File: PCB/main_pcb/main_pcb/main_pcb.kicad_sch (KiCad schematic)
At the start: 51 parts, among them J1 Conn_01x20_Socket, J2 Conn_01x20_Socket, J3 Conn_01x09_Socket, SW0_Header1 B6B-XH-A, SW1_Header1 B6B-XH-A

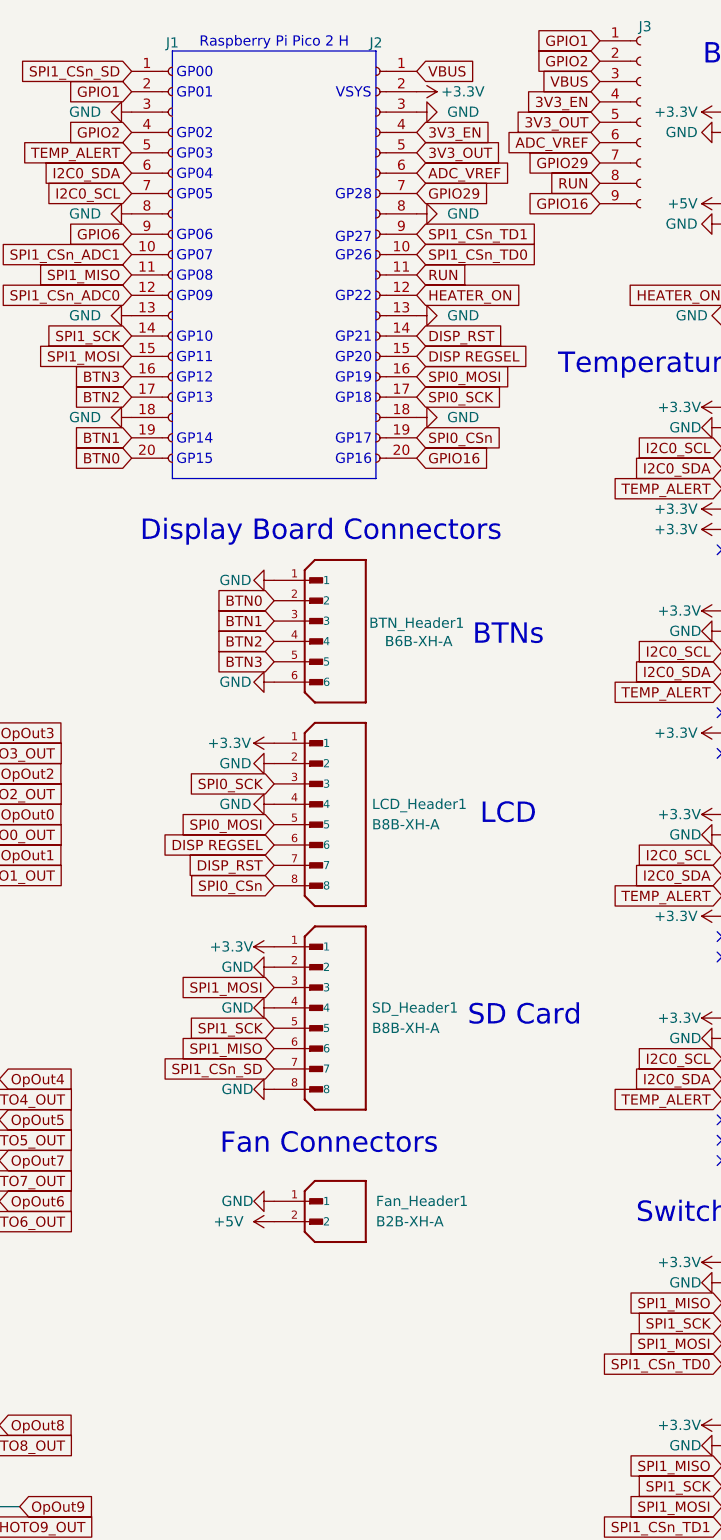
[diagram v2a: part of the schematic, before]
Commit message: Fully seperated analog ground from digital ground on the main PCB.
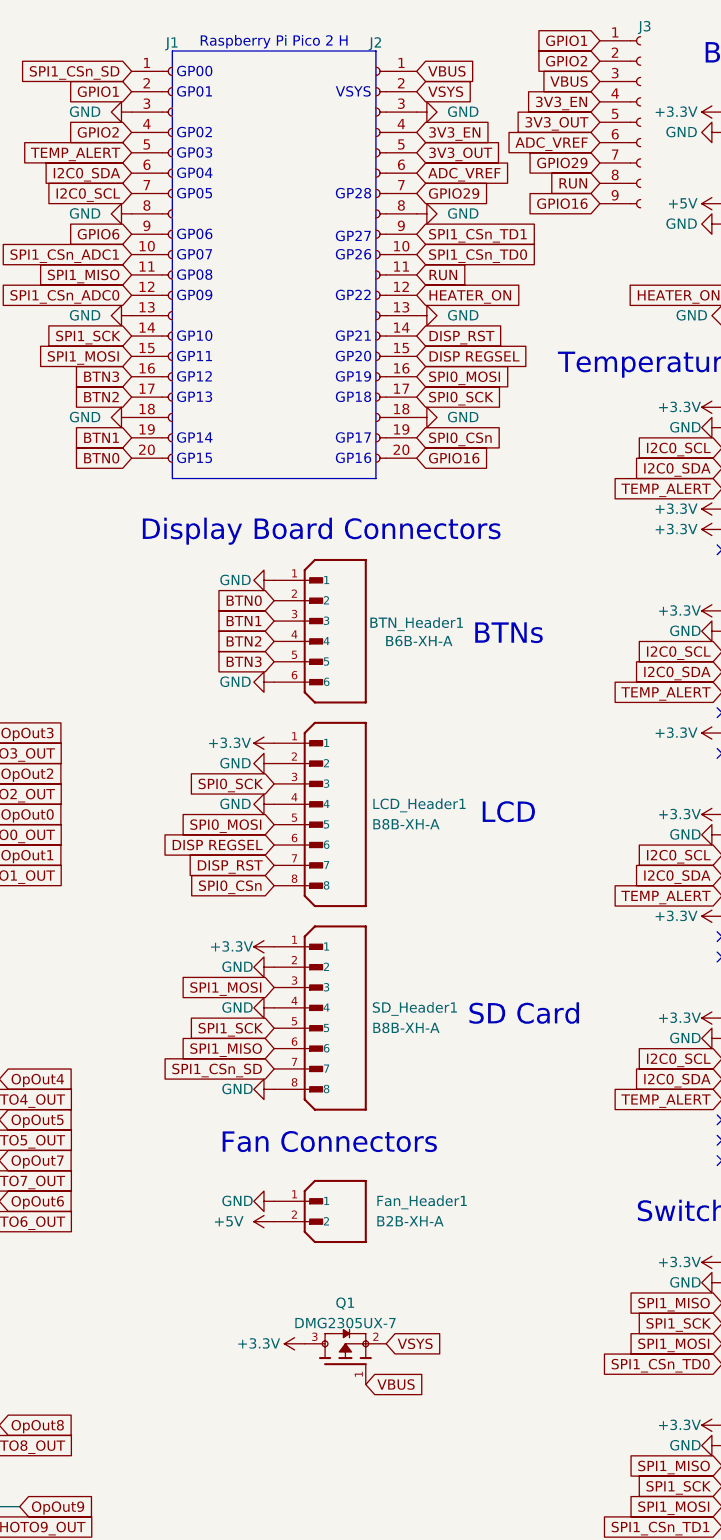
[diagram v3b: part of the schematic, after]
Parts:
- added Q1: DMG2305UX-7, DMG2305UX_7:SOT91P240X110-3N_DMG2305UX-7, symbol DMG2305UX-7:DMG2305UX-7
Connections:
- net +3.3V: now also Q1.3; no longer J2.2 (Pin_2)
- net VBUS: now also Q1.1
- new net VSYS: J2.2 (Pin_2), Q1.2
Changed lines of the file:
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@@
 		)
 	)
+	(global_label "VSYS"
+		(shape input)
+		(at 330.2 21.59 0)
+		(fields_autoplaced yes)
+		(effects
+			(font
+				(size 1.27 1.27)
+			)
+			(justify left)
+		)
+		(property "Intersheetrefs" "${INTERSHEET_REFS}"
+			(at 337.7814 21.59 0)
+			(effects
+				(font
+					(size 1.27 1.27)
+				)
+				(justify left)
+				(hide yes)
+			)
+		)
+	)
 	(global_label "SPI0_SCK"
 		(shape input)
@@
 		)
 	)
+	(global_label "VSYS"
+		(shape input)
+		(at 326.39 177.8 0)
+		(fields_autoplaced yes)
+		(effects
+			(font
+				(size 1.27 1.27)
+			)
+			(justify left)
+		)
+		(property "Intersheetrefs" "${INTERSHEET_REFS}"
+			(at 333.9714 177.8 0)
+			(effects
+				(font
+					(size 1.27 1.27)
+				)
+				(justify left)
+				(hide yes)
+			)
+		)
+	)
 	(global_label "OpIn7"
 		(shape input)
@@
 		)
 	)
+	(global_label "VBUS"
+		(shape input)
+		(at 323.85 182.88 0)
+		(fields_autoplaced yes)
+		(effects
+			(font
+				(size 1.27 1.27)
+			)
+			(justify left)
+		)
+		(property "Intersheetrefs" "${INTERSHEET_REFS}"
+			(at 331.7338 182.88 0)
+			(effects
+				(font
+					(size 1.27 1.27)
+				)
+				(justify left)
+				(hide yes)
+			)
+		)
+	)
 	(global_label "PHOTO6_OUT"
 		(shape input)
@@
 	)
 	(symbol
+		(lib_id "DMG2305UX-7:DMG2305UX-7")
+		(at 321.31 180.34 90)
+		(unit 1)
+		(exclude_from_sim no)
+		(in_bom yes)
+		(on_board yes)
+		(dnp no)
+		(fields_autoplaced yes)
+		(property "Reference" "Q1"
+			(at 321.31 172.72 90)
+			(effects
+				(font
+					(size 1.27 1.27)
+				)
+			)
+		)
+		(property "Value" "DMG2305UX-7"
+			(at 321.31 175.26 90)
+			(effects
+				(font
+					(size 1.27 1.27)
+				)
+			)
+		)
+		(property "Footprint" "DMG2305UX_7:SOT91P240X110-3N_DMG2305UX-7"
+			(at 321.31 180.34 0)
+			(effects
+				(font
+					(size 1.27 1.27)
+				)
+				(justify bottom)
+				(hide yes)
+			)
+		)
+		(property "Datasheet" ""
+			(at 321.31 180.34 0)
+			(effects
+				(font
+					(size 1.27 1.27)
+				)
+				(hide yes)
+			)
+		)
+		(property "Description" ""
+			(at 321.31 180.34 0)
+			(effects
+				(font
+					(size 1.27 1.27)
+				)
+				(hide yes)
+			)
+		)
+		(property "PARTREV" "09/2018"
+			(at 321.31 180.34 0)
+			(effects
+				(font
+					(size 1.27 1.27)
+				)
+				(justify bottom)
+				(hide yes)
+			)
+		)
+		(property "MANUFACTURER" "Diodes Inc."
+			(at 321.31 180.34 0)
+			(effects
+				(font
+					(size 1.27 1.27)
+				)
+				(justify bottom)
+				(hide yes)
+			)
+		)
+		(property "MAXIMUM_PACKAGE_HEIGHT" "1.1mm"
+			(at 321.31 180.34 0)
+			(effects
+				(font
+					(size 1.27 1.27)
+				)
+				(justify bottom)
+				(hide yes)
+			)
+		)
+		(property "STANDARD" "IPC-7351B"
+			(at 321.31 180.34 0)
+			(effects
+				(font
+					(size 1.27 1.27)
+				)
+				(justify bottom)
+				(hide yes)
+			)
+		)
+		(pin "2"
+		)
+		(pin "3"
+		)
+		(pin "1"
+		)
+		(instances
+			(project ""
+				(path "/9e1b86fa-37cc-48d2-968d-4a7578d4873f"
+					(reference "Q1")
+					(unit 1)
+				)
+			)
+		)
+	)
+	(symbol
 		(lib_id "power:+3.3V")
 		(at 368.3 187.96 90)
@@
 	)
 	(symbol
+		(lib_id "power:+3V3")
+		(at 316.23 177.8 90)
+		(unit 1)
+		(exclude_from_sim no)
+		(in_bom yes)
+		(on_board yes)
+		(dnp no)
+		(property "Reference" "#PWR079"
+			(at 320.04 177.8 0)
+			(effects
+				(font
+					(size 1.27 1.27)
+				)
+				(hide yes)
+			)
+		)
+		(property "Value" "+3.3V"
+			(at 313.182 177.8 90)
+			(effects
+				(font
+					(size 1.27 1.27)
+				)
+				(justify left)
+			)
+		)
+		(property "Footprint" ""
+			(at 316.23 177.8 0)
+			(effects
+				(font
+					(size 1.27 1.27)
+				)
+				(hide yes)
+			)
+		)
+		(property "Datasheet" ""
+			(at 316.23 177.8 0)
+			(effects
+				(font
+					(size 1.27 1.27)
+				)
+				(hide yes)
+			)
+		)
+		(property "Description" "Power symbol creates a global label with name \"+3V3\""
+			(at 316.23 177.8 0)
+			(effects
+				(font
+					(size 1.27 1.27)
+				)
+				(hide yes)
+			)
+		)
+		(pin "1"
+		)
+		(instances
+			(project "main_pcb"
+				(path "/9e1b86fa-37cc-48d2-968d-4a7578d4873f"
+					(reference "#PWR079")
+					(unit 1)
+				)
+			)
+		)
+	)
+	(symbol
 		(lib_id "power:GND")
 		(at 222.25 124.46 270)
@@
 					(unit 1)
 				)
-			)
-		)
-	)
-	(symbol
-		(lib_id "power:+3V3")
-		(at 330.2 21.59 270)
-		(unit 1)
-		(exclude_from_sim no)
-		(in_bom yes)
-		(on_board yes)
-		(dnp no)
-		(property "Reference" "#PWR010"
-			(at 326.39 21.59 0)
-			(effects
-				(font
-					(size 1.27 1.27)
-				)
-				(hide yes)
-			)
-		)
-		(property "Value" "+3.3V"
-			(at 333.248 21.59 90)
-			(effects
-				(font
-					(size 1.27 1.27)
-				)
-				(justify left)
-			)
-		)
-		(property "Footprint" ""
-			(at 330.2 21.59 0)
-			(effects
-				(font
-					(size 1.27 1.27)
-				)
-				(hide yes)
-			)
-		)
-		(property "Datasheet" ""
-			(at 330.2 21.59 0)
-			(effects
-				(font
-					(size 1.27 1.27)
-				)
-				(hide yes)
-			)
-		)
-		(property "Description" "Power symbol creates a global label with name \"+3V3\""
-			(at 330.2 21.59 0)
-			(effects
-				(font
-					(size 1.27 1.27)
-				)
-				(hide yes)
-			)
-		)
-		(pin "1"
-		)
-		(instances
-			(project "main_pcb"
-				(path "/9e1b86fa-37cc-48d2-968d-4a7578d4873f"
-					(reference "#PWR010")
-					(unit 1)
-				)

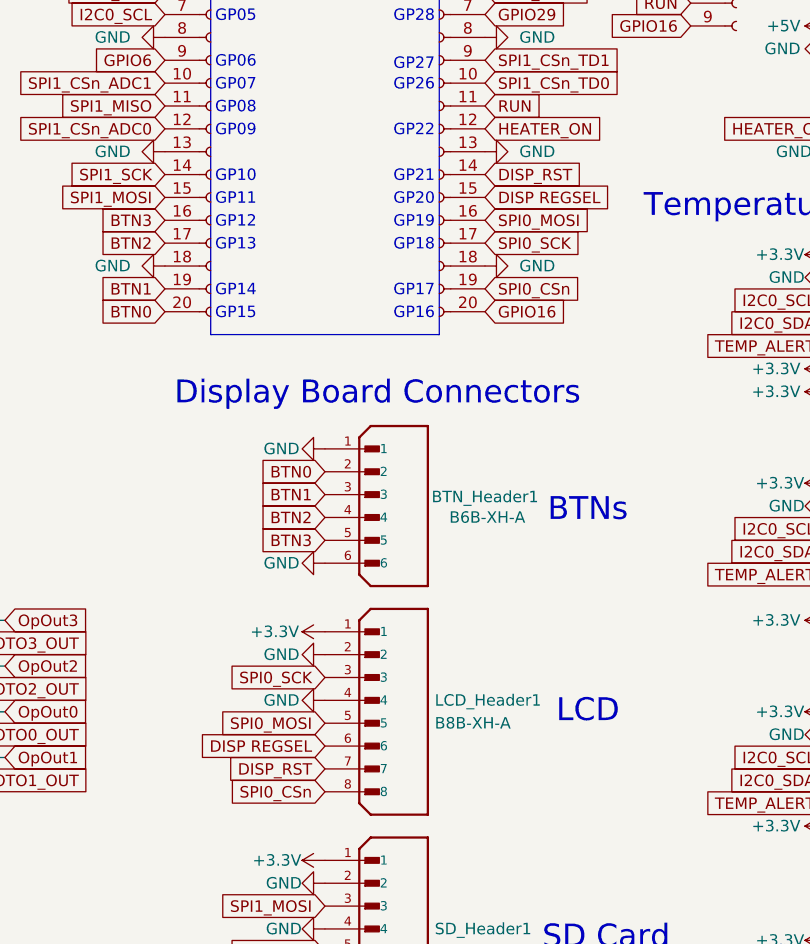
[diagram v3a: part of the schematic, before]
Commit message: Switched around regsel and reset pins for display header on main PCB.
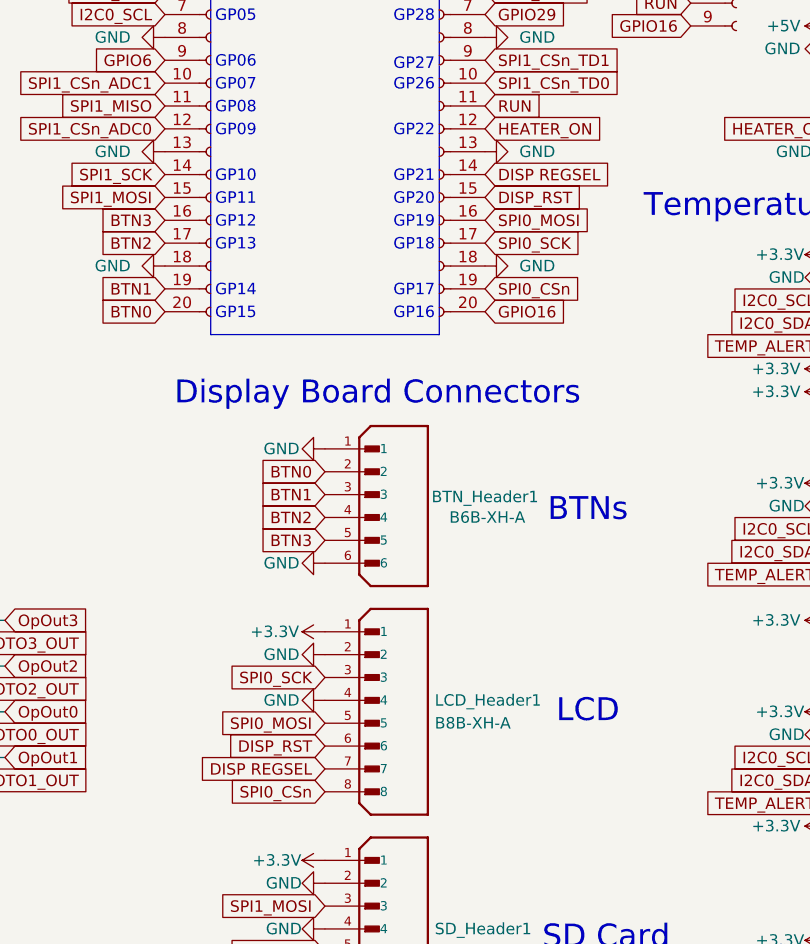
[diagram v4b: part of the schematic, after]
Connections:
- net DISP REGSEL: now also J2.14 (Pin_14), LCD_Header1.7; no longer J2.15 (Pin_15), LCD_Header1.6
- net DISP_RST: now also J2.15 (Pin_15), LCD_Header1.6; no longer J2.14 (Pin_14), LCD_Header1.7

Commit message: A lot of changes, display logic and some error handling
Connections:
- net DISP REGSEL renamed DISP RST
- net DISP_RST renamed DISP_A0
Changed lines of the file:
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@@
 		)
 	)
-	(global_label "DISP REGSEL"
+	(global_label "DISP RST"
 		(shape input)
 		(at 330.2 52.07 0)
@@
 		)
 		(property "Intersheetrefs" "${INTERSHEET_REFS}"
-			(at 345.5827 52.07 0)
+			(at 341.9542 52.07 0)
 			(effects
 				(font
@@
 		)
 	)
-	(global_label "DISP REGSEL"
+	(global_label "DISP RST"
 		(shape input)
 		(at 312.42 118.11 180)
@@
 		)
 		(property "Intersheetrefs" "${INTERSHEET_REFS}"
-			(at 297.0373 118.11 0)
+			(at 300.6658 118.11 0)
 			(effects
 				(font
@@
 		)
 	)
-	(global_label "DISP_RST"
+	(global_label "DISP_A0"
 		(shape input)
 		(at 330.2 54.61 0)
@@
 		)
 		(property "Intersheetrefs" "${INTERSHEET_REFS}"
-			(at 341.9542 54.61 0)
+			(at 340.8052 54.61 0)
 			(effects
 				(font
@@
 		)
 	)
-	(global_label "DISP_RST"
+	(global_label "DISP_A0"
 		(shape input)
 		(at 312.42 115.57 180)
@@
 		)
 		(property "Intersheetrefs" "${INTERSHEET_REFS}"
-			(at 300.6658 115.57 0)
-			(effects
-				(font
+			(at 301.8148 115.57 0)
+			(effects
+				(font
